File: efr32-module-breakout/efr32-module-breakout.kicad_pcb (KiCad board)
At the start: 2 copper layers, 28 x 36 mm, 12 parts, among them J1 Conn_01x06, J2 Conn_01x12, J3 Conn_01x12, SW1 SW_Push, U1 ZYZBP008

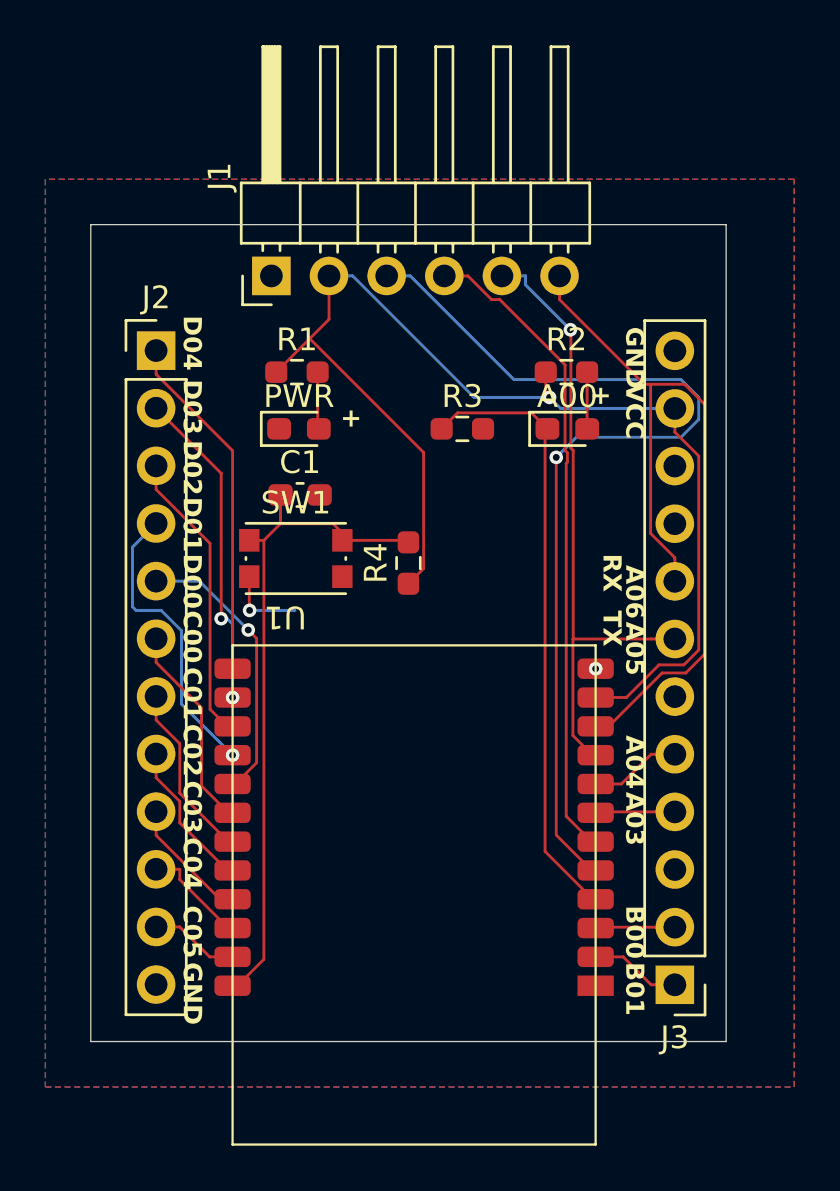
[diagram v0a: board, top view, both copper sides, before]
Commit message: change button footprint
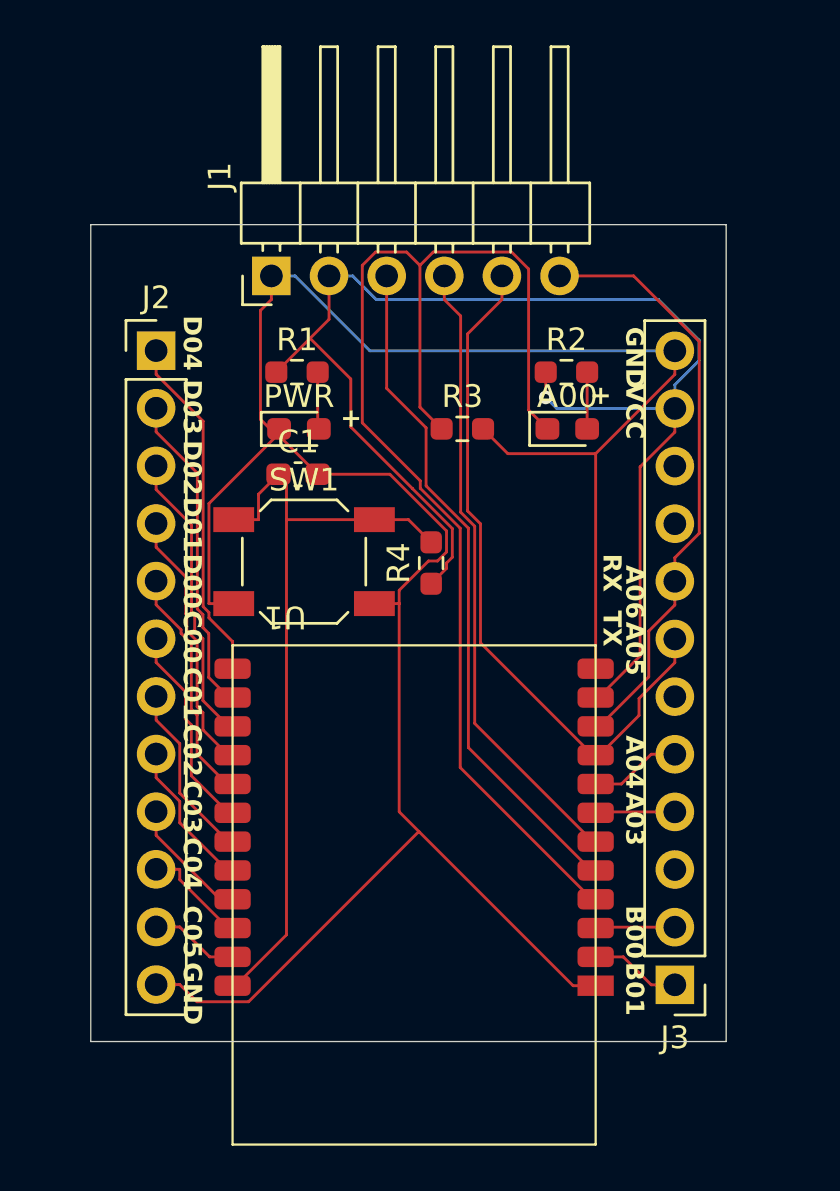
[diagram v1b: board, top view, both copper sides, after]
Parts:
- SW1: footprint Button_Switch_SMD:SW_Push_1P1T_NO_CK_KMR2 -> Button_Switch_SMD:SW_SPST_SKQG_WithoutStem
- moved R4 1.00 mm to (68.0, 60.9)
- moved C1 0.92 mm to (62.1, 57.0)
- moved SW1 0.39 mm to (62.4, 60.9)
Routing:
- net GND: track 3.49 -> 108.2 mm, vias 2 -> 0
- net usr_led: track 27.0 -> 55.7 mm
- net swdclk: track 42.9 -> 30.1 mm, vias 1 -> 0
- net rx: track 35.6 -> 26.3 mm
- net VCC: track 53.7 -> 61.2 mm
- net RST: track 29.6 -> 34.0 mm
- net tx: track 28.0 -> 30.8 mm, vias 1 -> 0
- net PD00: track 12.4 -> 10.5 mm, vias 1 -> 0
- net PD01: track 13.1 -> 11.7 mm, vias 1 -> 0
- net swdio: track 28.7 -> 27.8 mm
- net PD03: track 14.3 -> 14.2 mm, vias 2 -> 0
- removed copper zone on B.Cu, net GND
- removed copper zone on F.Cu, net GND

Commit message: adopt pcbway
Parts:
- A00, PWR: footprint LED_SMD:LED_0603_1608Metric_Pad1.05x0.95mm_HandSolder -> LED_SMD:LED_0603_1608Metric
- C1: footprint Capacitor_SMD:C_0603_1608Metric_Pad1.08x0.95mm_HandSolder -> Capacitor_SMD:C_0603_1608Metric
- R1, R2, R3, R4: footprint Resistor_SMD:R_0603_1608Metric_Pad0.98x0.95mm_HandSolder -> Resistor_SMD:R_0603_1608Metric
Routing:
- net usr_led: track 55.7 -> 27.4 mm
- net VCC: track 61.2 -> 47.6 mm
- net swdclk: track 30.1 -> 43.5 mm
- net rx: track 26.3 -> 29.8 mm
- net PD02: track 13.0 -> 14.5 mm, vias 0 -> 1
- net swdio: track 27.8 -> 28.8 mm
- net tx: track 30.8 -> 31.3 mm
- net GND: track 108.2 -> 107.8 mm, vias 0 -> 1
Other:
- rule solder_mask_min_width: 0.12 -> 0.1016
